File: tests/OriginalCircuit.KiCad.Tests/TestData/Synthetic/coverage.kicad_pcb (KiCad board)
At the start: 2 copper layers, 1 part, among them U1 TestFP

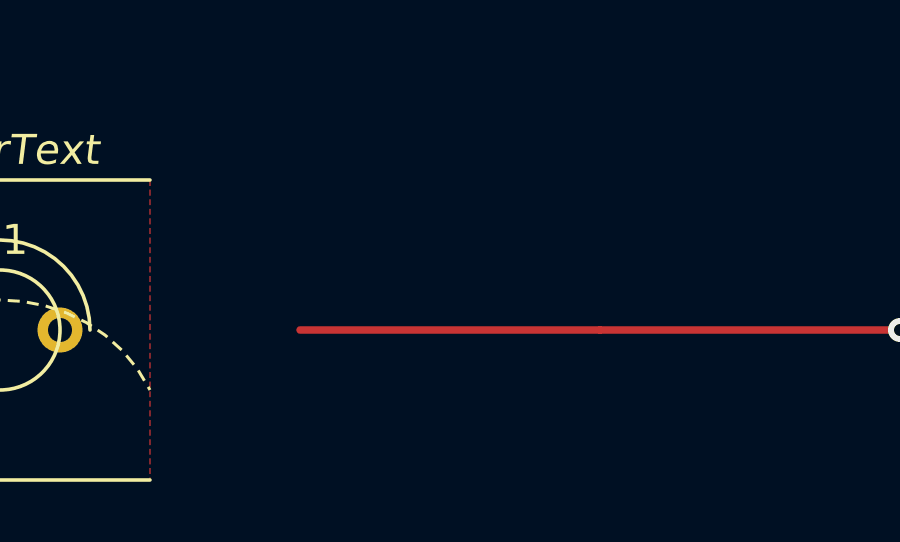
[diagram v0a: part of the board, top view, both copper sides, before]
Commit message: Remove all S-Expression caching from model classes, readers, and writers
Remove ~60 raw SExpression properties (SourceTree, *Raw, RenderCache,
RawNode, Instances, GeneratedElements) from all model classes. Update
all readers to stop caching raw S-expression subtrees and all writers
to serialize exclusively from typed model properties.

Add typed zone emission for connect_pads, fill, and keepout sections
that were previously only preserved via raw caching.

Delete DataFeatureRoundTripTests (verified raw property survival) and
remove raw-dependent assertions from other test files. Add zone with
hatch fill values to synthetic coverage test data. Update CLAUDE.md
with raw S-Expression caching policy.

Features without typed models (setup, layers, paper, title_block,
dimensions, groups, teardrops, images, embedded_files, etc.) are now
silently dropped on write, surfacing genuine model coverage gaps.
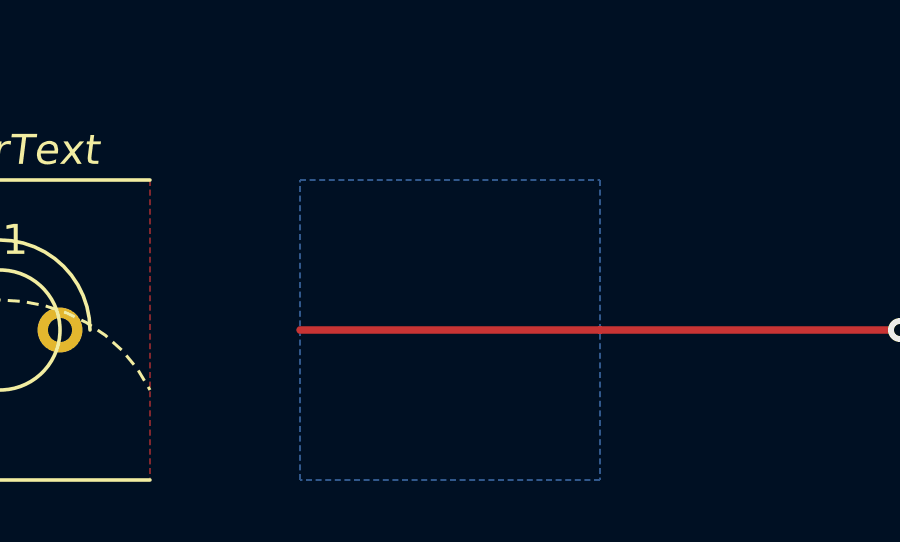
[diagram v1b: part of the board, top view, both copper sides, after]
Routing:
- added copper zone on B.Cu, net VCC
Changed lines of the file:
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@@
+    )
+  )
+  ;; Zone with hatch fill to cover hatch properties
+  (zone
+    (net 2)
+    (net_name "VCC")
+    (layer "B.Cu")
+    (hatch full 0.5)
+    (connect_pads
+      (clearance 0.3)
+    )
+    (min_thickness 0.2)
+    (fill yes
+      (thermal_gap 0.4)
+      (thermal_bridge_width 0.4)
+      (hatch_thickness 0.3)
+      (hatch_gap 0.4)
+      (hatch_orientation 45)
+      (hatch_smoothing_level 1)
+      (hatch_smoothing_value 0.2)
+      (hatch_border_algorithm 1)
+      (hatch_min_hole_area 0.5)
+    )
+    (polygon
+      (pts
+        (xy 110 95)
+        (xy 120 95)
+        (xy 120 105)
+        (xy 110 105)
+      )
     )
   )
